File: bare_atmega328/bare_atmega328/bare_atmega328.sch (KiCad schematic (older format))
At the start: 21 parts, among them J1 22-23-2021, J2 22-23-2021, J3 640456-3, J4 22-23-2021, J5 Conn_01x14_Male, J6 Conn_01x14_Male, J7 22-23-2021, SW1 SW_Push, U1 ATMEGA328-PU, U2 NE555DR, Y1 Crystal

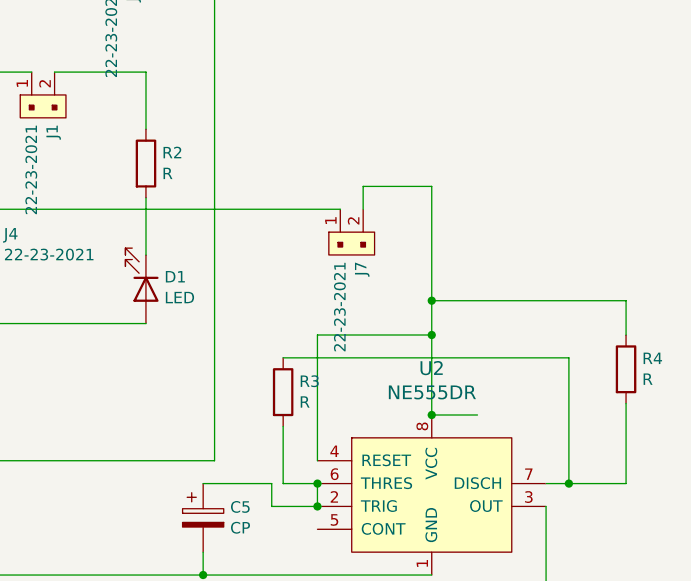
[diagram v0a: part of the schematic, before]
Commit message: Version v1.2 atmega328 + 555 timer
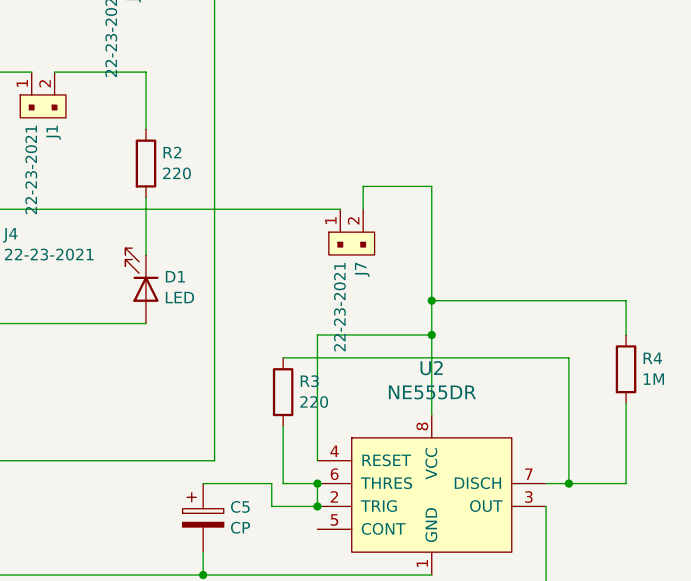
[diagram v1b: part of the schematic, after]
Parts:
- D1: footprint LED_SMD:LED_1210_3225Metric_Pad1.42x2.65mm_HandSolder -> LED_SMD:LED_0603_1608Metric_Pad1.05x0.95mm_HandSolder
- R2, R3: value R -> 220
- R4: value R -> 1M
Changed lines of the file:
@@
 encoding utf-8
 Sheet 1 1
-Title ""
+Title "Atmega328 + 555"
 Date ""
-Rev ""
+Rev "V1.2"
 Comp ""
 Comment1 ""
 Comment2 ""
 Comment3 ""
-Comment4 ""
+Comment4 "Jose Areas"
 $EndDescr
 $Comp
@@
 F 0 "D1" V 8347 5180 50  0000 L CNN
 F 1 "LED" V 8438 5180 50  0000 L CNN
-F 2 "LED_SMD:LED_1210_3225Metric_Pad1.42x2.65mm_HandSolder" H 8400 5100 50  0001 C CNN
+F 2 "LED_SMD:LED_0603_1608Metric_Pad1.05x0.95mm_HandSolder" H 8400 5100 50  0001 C CNN
 F 3 "~" H 8400 5100 50  0001 C CNN
 	1    8400 5100
@@
 P 8400 4550
 F 0 "R2" H 8470 4596 50  0000 L CNN
-F 1 "R" H 8470 4505 50  0000 L CNN
+F 1 "220" H 8470 4505 50  0000 L CNN
 F 2 "Resistor_THT:R_Axial_DIN0204_L3.6mm_D1.6mm_P7.62mm_Horizontal" V 8330 4550 50  0001 C CNN
 F 3 "~" H 8400 4550 50  0001 C CNN
@@
 P 10500 5450
 F 0 "R4" H 10570 5496 50  0000 L CNN
-F 1 "R" H 10570 5405 50  0000 L CNN
+F 1 "1M" H 10570 5405 50  0000 L CNN
 F 2 "Resistor_THT:R_Axial_DIN0204_L3.6mm_D1.6mm_P7.62mm_Horizontal" V 10430 5450 50  0001 C CNN
 F 3 "~" H 10500 5450 50  0001 C CNN
@@
 P 9000 5550
 F 0 "R3" H 9070 5596 50  0000 L CNN
-F 1 "R" H 9070 5505 50  0000 L CNN
+F 1 "220" H 9070 5505 50  0000 L CNN
 F 2 "Resistor_THT:R_Axial_DIN0204_L3.6mm_D1.6mm_P7.62mm_Horizontal" V 8930 5550 50  0001 C CNN
 F 3 "~" H 9000 5550 50  0001 C CNN
@@
 	7550 4750 7550 4850
 Wire Wire Line
-	9850 5650 9650 5650
-Connection ~ 9650 5650
-Wire Wire Line
 	9000 5400 10250 5400
